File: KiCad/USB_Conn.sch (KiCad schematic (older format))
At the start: 5 parts

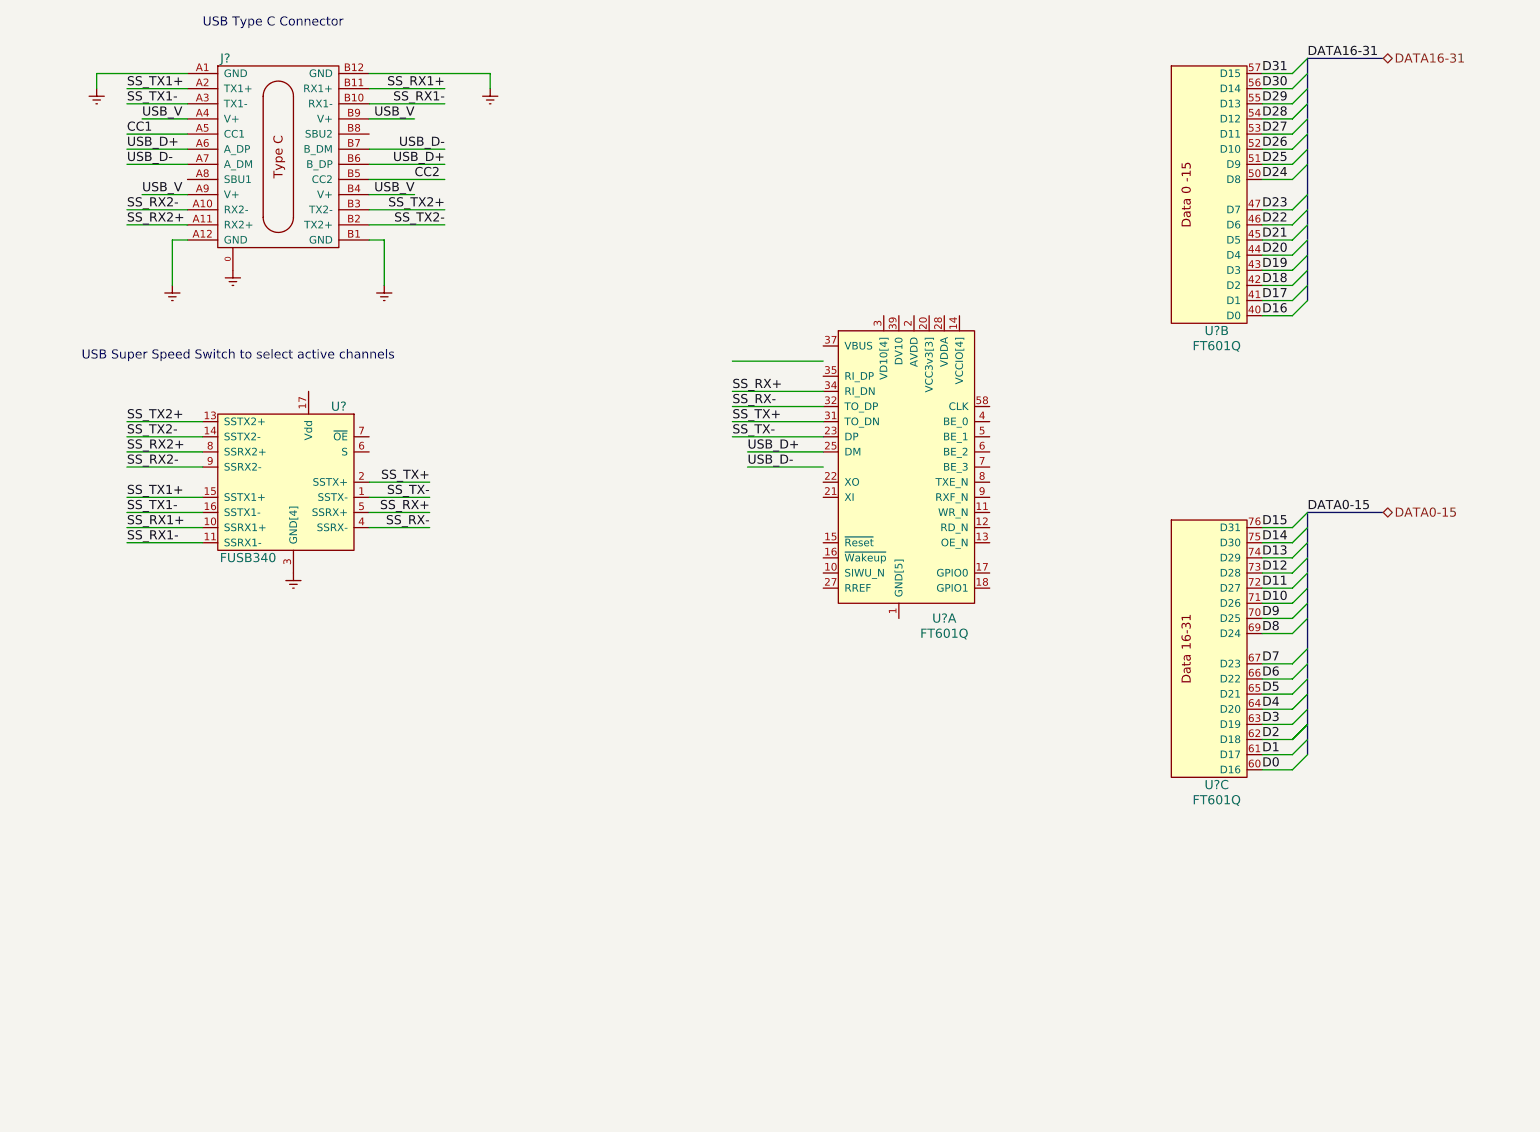
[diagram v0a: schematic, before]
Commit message: added current sense&switch
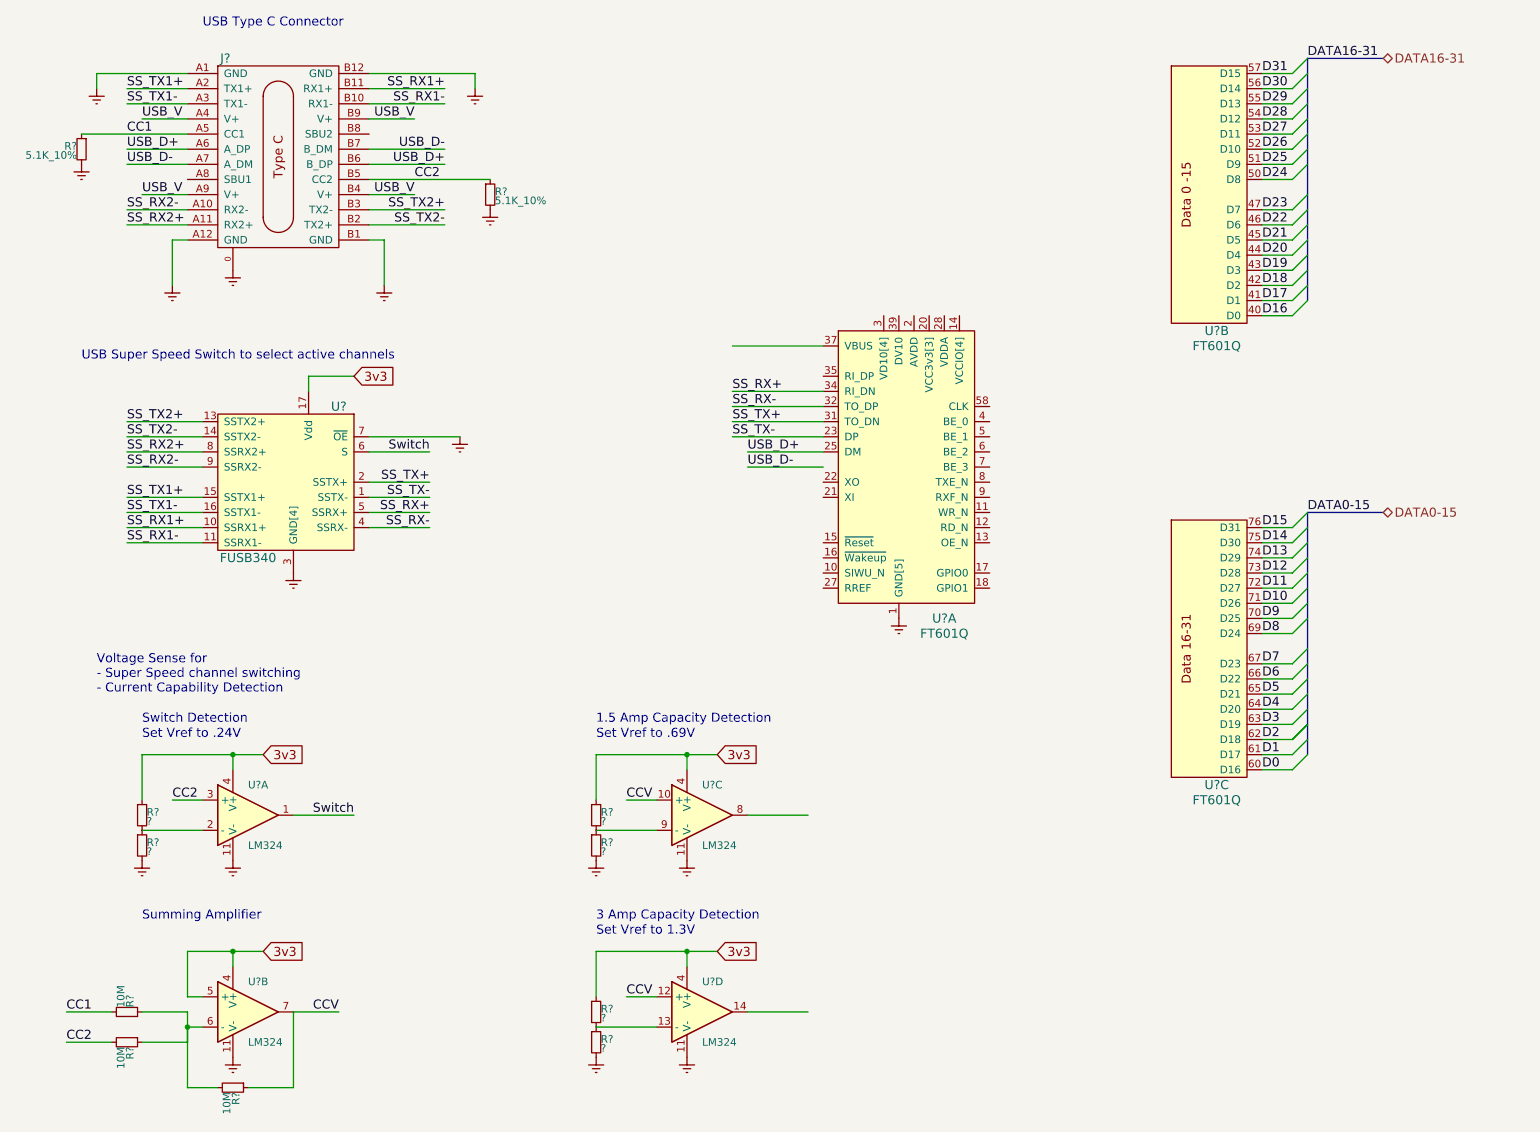
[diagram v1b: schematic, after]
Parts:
- added R? (x2): 5.1K_10%, symbol R_Small
- added R? (x6): ?, symbol R_Small
- added R? (x3): 10M, symbol R_Small
- added U? (x4): LM324, symbol LM324
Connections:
- net labels added: 3v3, CCV, Switch
- wire segments 78 -> 120
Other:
- note added: "1.5 Amp Capacity Detection"
- note added: "3 Amp Capacity Detection"
- note added: "Set Vref to .24V"
- note added: "Set Vref to .69V"
- note added: "Set Vref to 1.3V"
- note added: "Summing Amplifier"
- note added: "Switch Detection"
- note added: "Voltage Sense for\n- Super Speed channel switching\n- Current Capability Detection"

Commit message: more sheets
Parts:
- removed R? (x3): 10M, symbol R_Small
- added RN?: 1M, symbol R_Pack04
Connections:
- net 3v3: no longer U?.5 (+)
- net CC1: now also RN?.1 (R1.1)
- net CC2: now also RN?.2 (R2.1)
- net CCV: now also RN?.4 (R4.1)
- net Earth: now also RN?.3 (R3.1)
- net CLK: now reaches U?.58 (CLK)
- net at U?.6 (-): now also RN?.5 (R4.2), RN?.6 (R3.2)
- net 1.5A_DET: now reaches U?.8
- net 3A_DET: now reaches U?.14
- new net: RN?.7 (R2.2), RN?.8 (R1.2), U?.5 (+)
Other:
- moved on the sheet: R?, U?C, U?D

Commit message: added connections
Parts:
- removed R? (x2): ?, symbol R_Small
- added C1, C2, C3, C4, C5: .1u, symbol C_Small
- added C6, C7: 18p, symbol C_Small
- added C8: 4.7uF, Capacitors_SMD:C_0603, symbol C_Small
- added R7: 10K, symbol R_Small
- added R8: 1.6K 1%, symbol R_Small
- added Y1: 30MHz, symbol Crystal_Small
- gave numbers to parts that had none: 11
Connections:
- net 3v3 is gone; now on net VCC3v3: R2.1, R4.1, U1.4 (V+), U1.4 (V+), U1.4 (V+), U1.4 (V+), U3.17 (Vdd)
- net VCCIO is gone; now on net VCC3v3: U4.14 (VCCIO[4]), U4.49 (VCCIO), U4.59 (VCCIO), U4.68 (VCCIO)
- net CC1: now also U1.2 (-)
- net Earth: now also C5.1, C6.2, C7.1, C8.2, R8.2
- net SS_RX+: now also U4.35 (RI_DP); no longer U4.34 (RI_DN)
- net SS_RX-: now also U4.34 (RI_DN); no longer U4.32 (TO_DP)
- net SS_TX+: now also U4.32 (TO_DP); no longer U4.31 (TO_DN)
- net SS_TX-: now also U4.31 (TO_DN); no longer U4.23 (DP)
- net SS_TX1+: now also C4.2; no longer U3.15 (SSTX1+)
- net SS_TX1-: now also C2.1; no longer U3.16 (SSTX1-)
- net SS_TX2+: now also C3.2; no longer U3.13 (SSTX2+)
- net SS_TX2-: now also C1.1; no longer U3.14 (SSTX2-)
- net USB_D+: now also U4.23 (DP); no longer U4.25 (DM)
- net USB_D-: now also U4.25 (DM)
- net VCC3v3: now also U4.28 (VDDA), R7.1
- net VD10: now also U4.2 (AVDD), U4.39 (DV10), C8.1
- net ~SIWU: now reaches U4.10 (SIWU_N)
- net ~WR: now reaches U4.11 (WR_N)
- net ~RD: now reaches U4.12 (RD_N)
- net ~OE: now reaches U4.13 (OE_N)
- net ~Reset: now reaches U4.15 (~Reset)
- net ~Reset: now also C5.2, R7.2
- net ~Wakeup: now reaches U4.16 (~Wakeup)
- net GPIO0: now reaches U4.17 (GPIO0)
- net GPIO1: now reaches U4.18 (GPIO1)
- net at U4.21 (XI): now also C7.2, Y1.1
- net at U4.22 (XO): now also C6.1, Y1.2
- net at U4.27 (RREF): now also R8.1
- net BE_0: now reaches U4.4 (BE_0)
- net BE_1: now reaches U4.5 (BE_1)
- net BE_2: now reaches U4.6 (BE_2)
- net BE_3: now reaches U4.7 (BE_3)
- net ~TXE: now reaches U4.8 (TXE_N)
- net ~RXF: now reaches U4.9 (RXF_N)
- new net: C3.1, U3.13 (SSTX2+)
- new net: C1.2, U3.14 (SSTX2-)
- new net: C4.1, U3.15 (SSTX1+)
- new net: C2.2, U3.16 (SSTX1-)
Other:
- moved on the sheet: U3, U4A, U4B, U4C

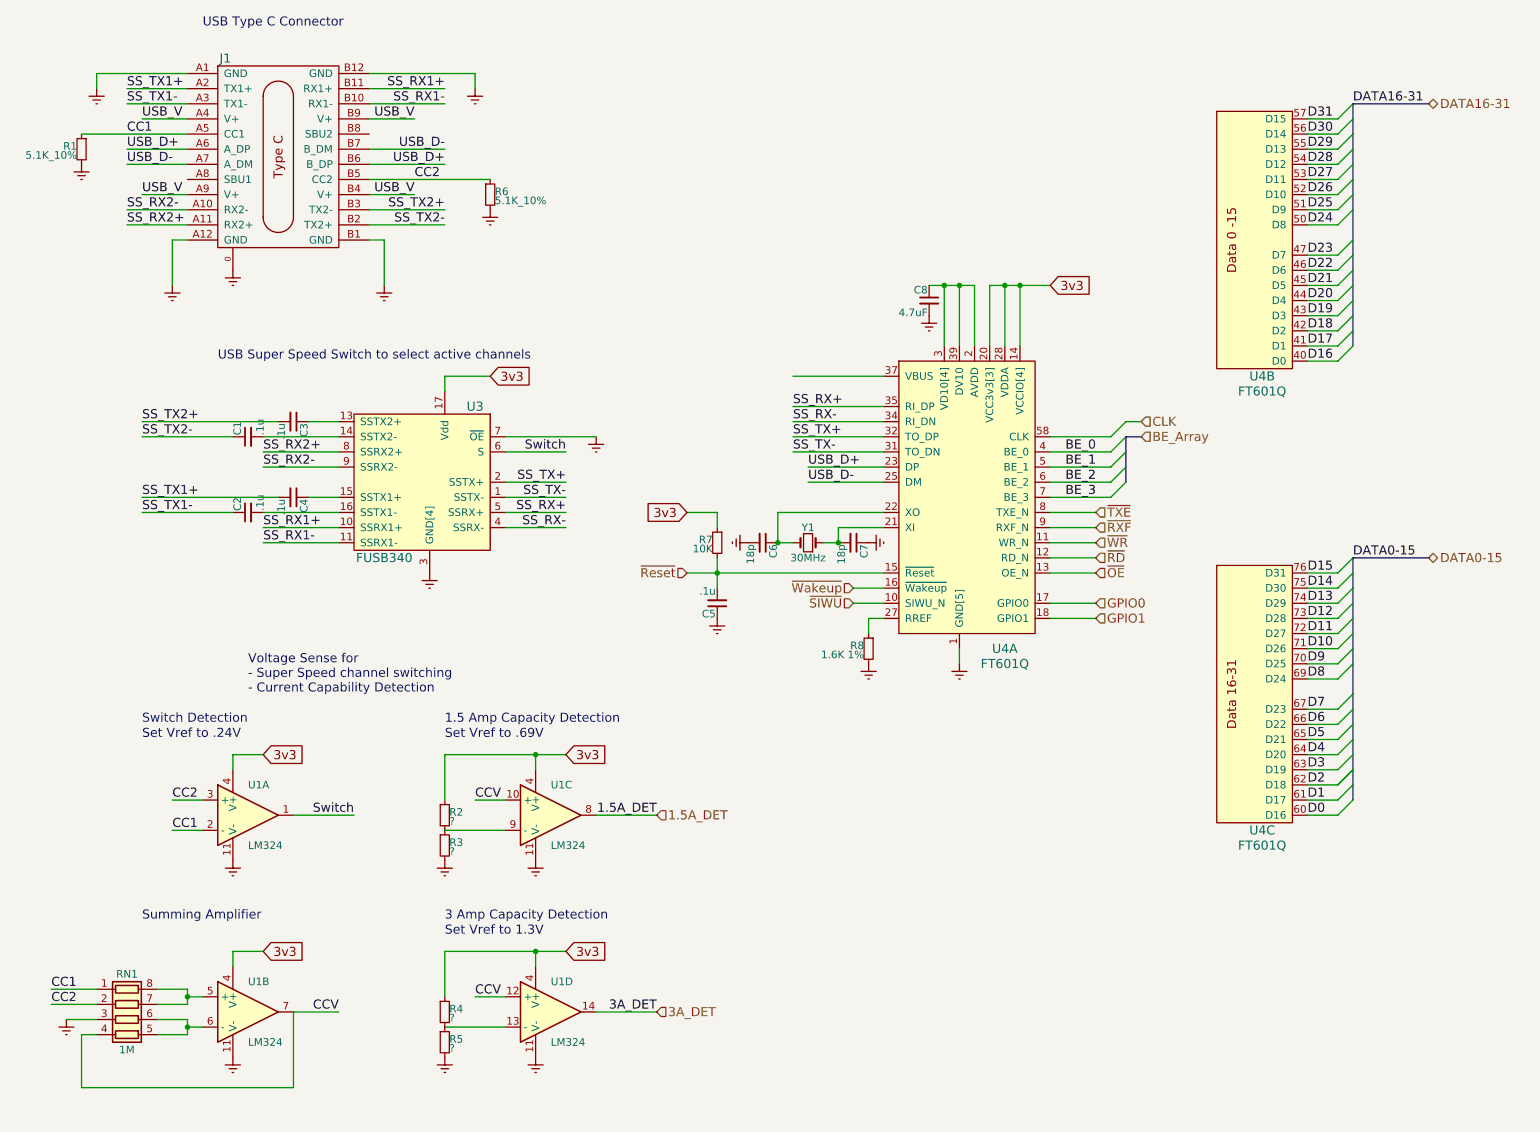
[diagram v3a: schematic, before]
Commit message: fix bus route
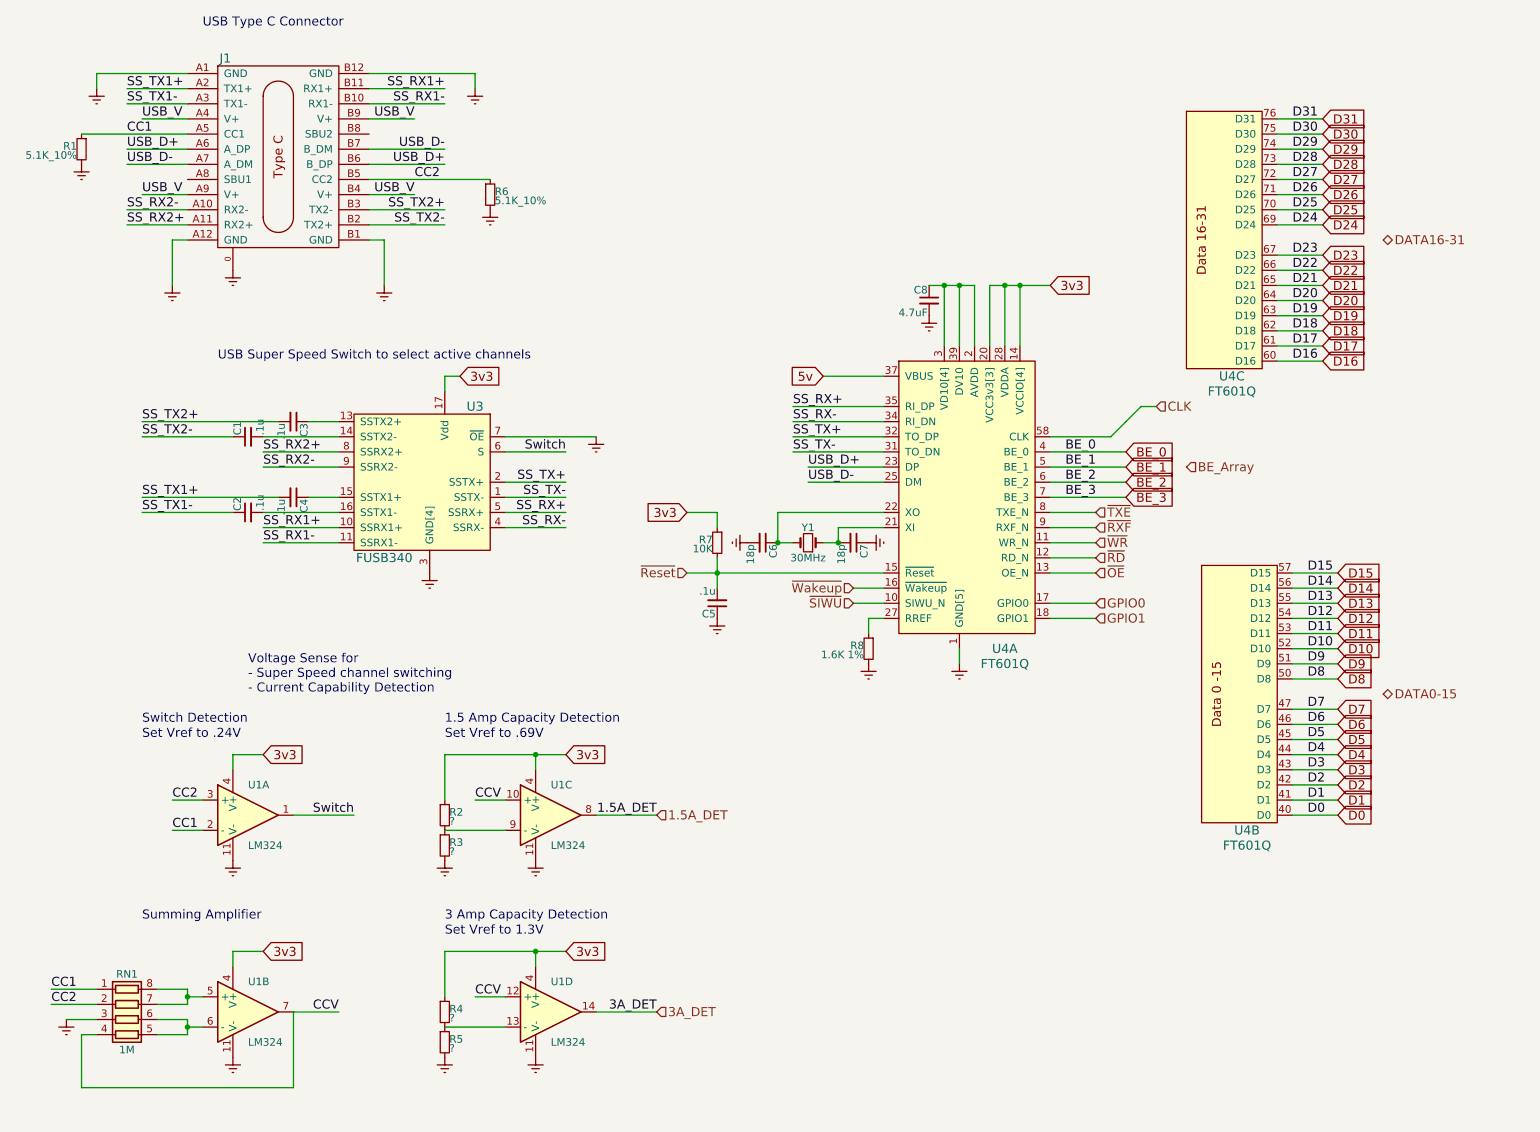
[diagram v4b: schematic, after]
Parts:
- U1: footprint (none) -> SMD_Packages:SOIC-14_N
- U4: footprint (none) -> Homebrew:QFN_76_PAD
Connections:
- net D0: now also U4.40 (D0); no longer U4.60 (D16)
- net D1: now also U4.41 (D1); no longer U4.61 (D17)
- net D10: now also U4.52 (D10); no longer U4.71 (D26)
- net D11: now also U4.53 (D11); no longer U4.72 (D27)
- net D12: now also U4.54 (D12); no longer U4.73 (D28)
- net D13: now also U4.55 (D13); no longer U4.74 (D29)
- net D14: now also U4.56 (D14); no longer U4.75 (D30)
- net D15: now also U4.57 (D15); no longer U4.76 (D31)
- net D16: now also U4.60 (D16); no longer U4.40 (D0)
- net D17: now also U4.61 (D17); no longer U4.41 (D1)
- net D18: now also U4.62 (D18); no longer U4.42 (D2)
- net D19: now also U4.63 (D19); no longer U4.43 (D3)
- net D2: now also U4.42 (D2); no longer U4.62 (D18)
- net D20: now also U4.64 (D20); no longer U4.44 (D4)
- net D21: now also U4.65 (D21); no longer U4.45 (D5)
- net D22: now also U4.66 (D22); no longer U4.46 (D6)
- net D23: now also U4.67 (D23); no longer U4.47 (D7)
- net D24: now also U4.69 (D24); no longer U4.50 (D8)
- net D25: now also U4.70 (D25); no longer U4.51 (D9)
- net D26: now also U4.71 (D26); no longer U4.52 (D10)
- net D27: now also U4.72 (D27); no longer U4.53 (D11)
- net D28: now also U4.73 (D28); no longer U4.54 (D12)
- net D29: now also U4.74 (D29); no longer U4.55 (D13)
- net D3: now also U4.43 (D3); no longer U4.63 (D19)
- net D30: now also U4.75 (D30); no longer U4.56 (D14)
- net D31: now also U4.76 (D31); no longer U4.57 (D15)
- net D4: now also U4.44 (D4); no longer U4.64 (D20)
- net D5: now also U4.45 (D5); no longer U4.65 (D21)
- net D6: now also U4.46 (D6); no longer U4.66 (D22)
- net D7: now also U4.47 (D7); no longer U4.67 (D23)
- net D8: now also U4.50 (D8); no longer U4.69 (D24)
- net D9: now also U4.51 (D9); no longer U4.70 (D25)
- net 5v: now reaches U4.37 (VBUS)
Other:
- moved on the sheet: U4B, U4C

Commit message: top routed?
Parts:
- C1, C2, C3, C4, C5, C6, C7: footprint (none) -> Capacitors_SMD:C_0402
- R1, R2, R3, R4, R5, R6, R7, R8: footprint (none) -> Resistors_SMD:R_0402
- RN1: footprint (none) -> Resistors_SMD:R_Array_Concave_4x0402
- Y1: footprint (none) -> Crystals:Crystal_SMD_MicroCrystal_CC1V-T1A-2pin_8.0x3.7mm
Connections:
- net SS_RX2+: no longer J1.A11 (RX2+)
- net SS_RX2-: no longer J1.A10 (RX2-)
- net SS_RX+ renamed SS_RX_P
- net SS_RX- renamed SS_RX_N
- net SS_RX1+ renamed SS_RX1_P
- net SS_RX1- renamed SS_RX1_N
- net SS_TX+ renamed SS_TX_P
- net SS_TX- renamed SS_TX_N
- net SS_TX1+ renamed SS_TX1_P
- net SS_TX1- renamed SS_TX1_N
- net SS_TX2+ renamed SS_TX2_P
- net SS_TX2- renamed SS_TX2_N
- net USB_D+ renamed USB_D_P
- net USB_D- renamed USB_D_N
- new net SS_RX2_N: J1.A10 (RX2-)
- new net SS_RX2_P: J1.A11 (RX2+)
